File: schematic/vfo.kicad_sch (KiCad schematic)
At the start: 12 parts, among them U2 Si5351-module

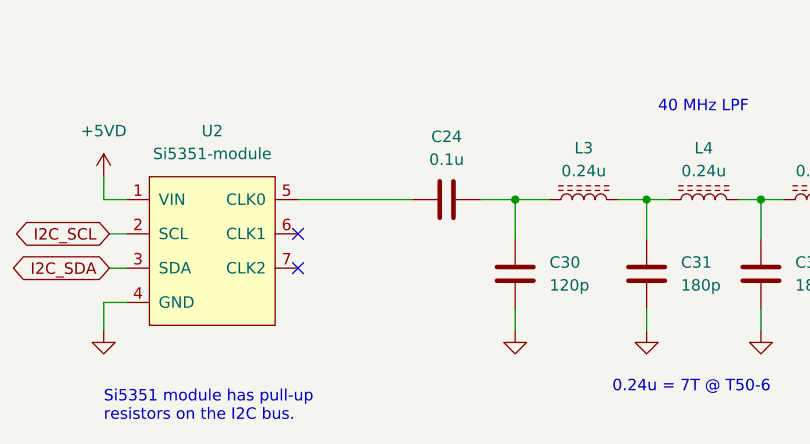
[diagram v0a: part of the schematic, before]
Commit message: Add CW tone generator + other changes
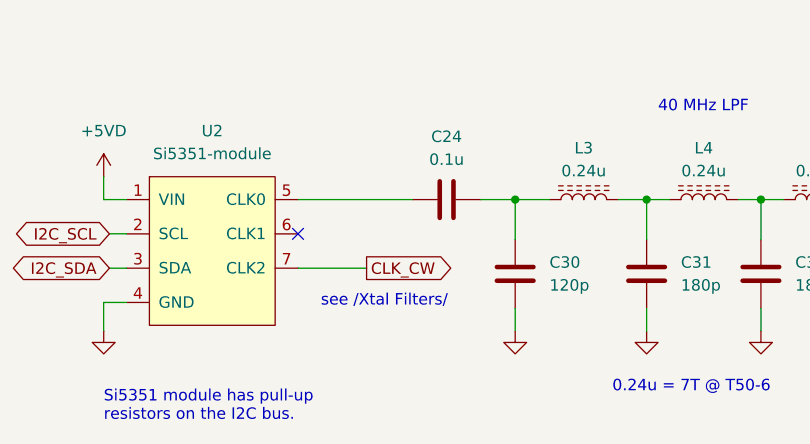
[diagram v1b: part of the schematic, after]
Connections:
- net CLK_CW: now reaches U2.7 (CLK2)
- no-connect marks 2 -> 1
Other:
- note added: "see /Xtal Filters/"
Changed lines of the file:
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@@
   )
   (no_connect (at 98.425 104.775))
-  (no_connect (at 98.425 108.585))
   (wire (pts (xy 98.425 100.965) (xy 111.125 100.965))
     (stroke (width 0) (type default))
@@
     (stroke (width 0) (type default))
   )
+  (wire (pts (xy 98.425 108.585) (xy 106.045 108.585))
+    (stroke (width 0) (type default))
+  )
   (wire (pts (xy 122.555 100.965) (xy 122.555 105.41))
     (stroke (width 0) (type default))
@@
     (effects (font (size 1.27 1.27)) (justify left bottom))
   )
+  (text "see /Xtal Filters/" (at 100.965 113.03 0)
+    (effects (font (size 1.27 1.27)) (justify left bottom))
+  )
   (text "0.24u = 7T @ T50-6" (at 133.35 122.555 0)
     (effects (font (size 1.27 1.27)) (justify left bottom))
@@
     (effects (font (size 1.27 1.27)) (justify left bottom))
   )
+  (global_label "CLK_CW" (shape output) (at 106.045 108.585 0) (fields_autoplaced)
+    (effects (font (size 1.27 1.27)) (justify left))
+    (property "Intersheetrefs" "${INTERSHEET_REFS}" (at 116.2079 108.585 0)
+      (effects (font (size 1.27 1.27)) (justify left) hide)
+    )
+  )
   (global_label "VFO_TX" (shape output) (at 208.28 103.505 0) (fields_autoplaced)

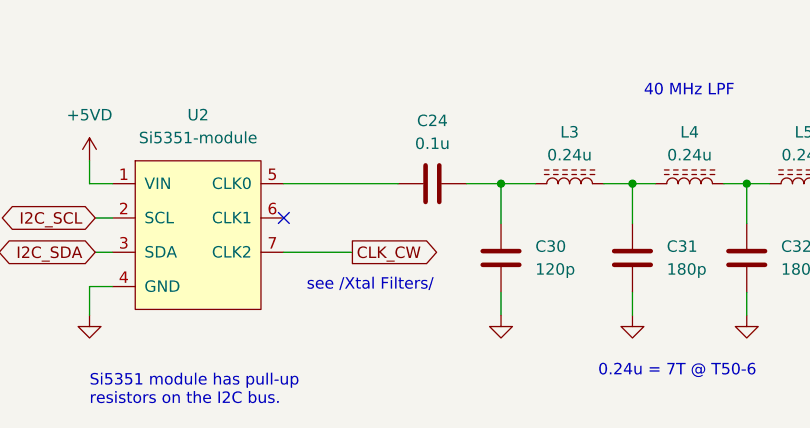
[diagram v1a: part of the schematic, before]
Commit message: Schematic: minor changes
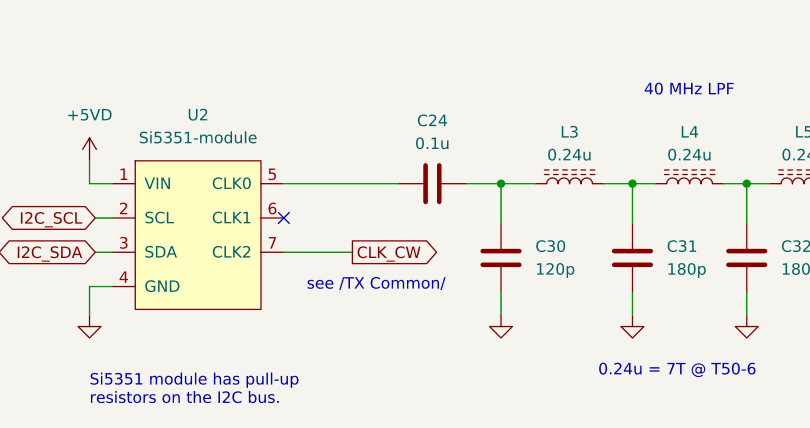
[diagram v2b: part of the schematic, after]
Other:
- note added: "see /TX Common/"
- note removed: "see /Xtal Filters/"
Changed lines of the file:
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@@
     (effects (font (size 1.27 1.27)) (justify left bottom))
   )
-  (text "see /Xtal Filters/" (at 100.965 113.03 0)
+  (text "see /TX Common/" (at 100.965 113.03 0)
     (effects (font (size 1.27 1.27)) (justify left bottom))
   )

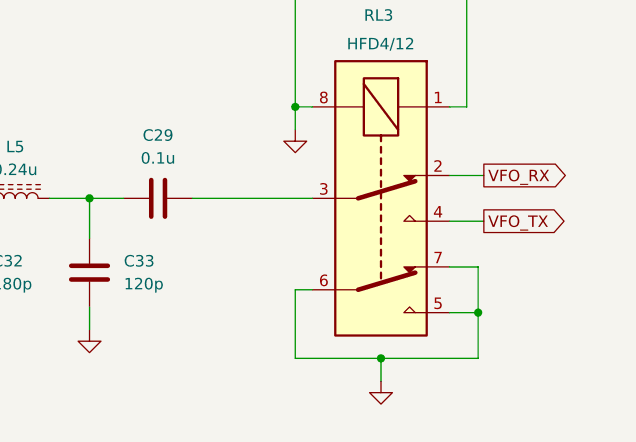
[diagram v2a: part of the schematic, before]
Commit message: Connect relay contact groups in parallel where appropriate
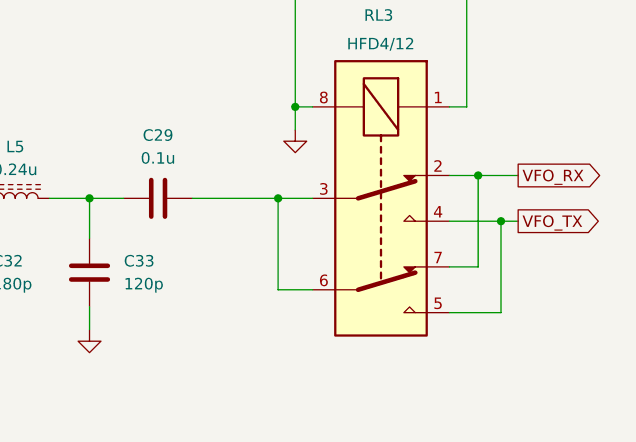
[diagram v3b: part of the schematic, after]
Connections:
- net GND: no longer RL3.5, RL3.6, RL3.7
- net VFO_RX: now also RL3.7
- net VFO_TX: now also RL3.5
- net at C29.2, RL3.3: now also RL3.6
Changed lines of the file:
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@@
   (junction (at 164.465 100.965) (diameter 0) (color 0 0 0 0)
   )
+  (junction (at 185.42 100.965) (diameter 0) (color 0 0 0 0)
+  )
+  (junction (at 207.645 98.425) (diameter 0) (color 0 0 0 0)
+  )
   (junction (at 122.555 100.965) (diameter 0) (color 0 0 0 0)
   )
-  (junction (at 196.85 118.745) (diameter 0) (color 0 0 0 0)
-  )
   (junction (at 137.16 100.965) (diameter 0) (color 0 0 0 0)
   )
+  (junction (at 210.185 103.505) (diameter 0) (color 0 0 0 0)
+  )
   (junction (at 206.375 76.2) (diameter 0) (color 0 0 0 0)
-  )
-  (junction (at 207.645 113.665) (diameter 0) (color 0 0 0 0)
   )
   (junction (at 187.325 90.805) (diameter 0) (color 0 0 0 0)
@@
     (stroke (width 0) (type default))
   )
-  (wire (pts (xy 204.47 113.665) (xy 207.645 113.665))
+  (wire (pts (xy 207.645 98.425) (xy 207.645 108.585))
+    (stroke (width 0) (type default))
+  )
+  (wire (pts (xy 204.47 113.665) (xy 210.185 113.665))
     (stroke (width 0) (type default))
   )
@@
     (stroke (width 0) (type default))
   )
-  (wire (pts (xy 207.645 113.665) (xy 207.645 108.585))
-    (stroke (width 0) (type default))
-  )
-  (wire (pts (xy 175.895 100.965) (xy 189.23 100.965))
+  (wire (pts (xy 175.895 100.965) (xy 185.42 100.965))
+    (stroke (width 0) (type default))
+  )
+  (wire (pts (xy 207.645 98.425) (xy 212.09 98.425))
     (stroke (width 0) (type default))
   )
@@
     (stroke (width 0) (type default))
   )
-  (wire (pts (xy 196.85 118.745) (xy 207.645 118.745))
-    (stroke (width 0) (type default))
-  )
   (wire (pts (xy 206.375 62.23) (xy 206.375 76.2))
     (stroke (width 0) (type default))
   )
-  (wire (pts (xy 187.325 118.745) (xy 187.325 111.125))
-    (stroke (width 0) (type default))
-  )
   (wire (pts (xy 206.375 62.23) (xy 210.82 62.23))
     (stroke (width 0) (type default))
@@
     (stroke (width 0) (type default))
   )
+  (wire (pts (xy 210.185 113.665) (xy 210.185 103.505))
+    (stroke (width 0) (type default))
+  )
   (wire (pts (xy 122.555 113.03) (xy 122.555 115.57))
     (stroke (width 0) (type default))
@@
     (stroke (width 0) (type default))
   )
-  (wire (pts (xy 196.85 121.285) (xy 196.85 118.745))
+  (wire (pts (xy 210.185 103.505) (xy 212.09 103.505))
+    (stroke (width 0) (type default))
+  )
+  (wire (pts (xy 185.42 100.965) (xy 189.23 100.965))
     (stroke (width 0) (type default))
   )
@@
     (stroke (width 0) (type default))
   )
-  (wire (pts (xy 187.325 111.125) (xy 189.23 111.125))
-    (stroke (width 0) (type default))
-  )
-  (wire (pts (xy 196.85 118.745) (xy 187.325 118.745))
-    (stroke (width 0) (type default))
-  )
-  (wire (pts (xy 204.47 98.425) (xy 208.28 98.425))
+  (wire (pts (xy 185.42 100.965) (xy 185.42 111.125))
+    (stroke (width 0) (type default))
+  )
+  (wire (pts (xy 185.42 111.125) (xy 189.23 111.125))
+    (stroke (width 0) (type default))
+  )
+  (wire (pts (xy 204.47 98.425) (xy 207.645 98.425))
     (stroke (width 0) (type default))
   )
@@
     (stroke (width 0) (type default))
   )
-  (wire (pts (xy 207.645 118.745) (xy 207.645 113.665))
-    (stroke (width 0) (type default))
-  )
-  (wire (pts (xy 204.47 103.505) (xy 208.28 103.505))
+  (wire (pts (xy 204.47 103.505) (xy 210.185 103.505))
     (stroke (width 0) (type default))
   )
@@
     )
   )
-  (global_label "VFO_TX" (shape output) (at 208.28 103.505 0) (fields_autoplaced)
-    (effects (font (size 1.27 1.27)) (justify left))
-    (property "Intersheetrefs" "${INTERSHEET_REFS}" (at 217.8382 103.505 0)
+  (global_label "VFO_TX" (shape output) (at 212.09 103.505 0) (fields_autoplaced)
+    (effects (font (size 1.27 1.27)) (justify left))
+    (property "Intersheetrefs" "${INTERSHEET_REFS}" (at 221.6482 103.505 0)
       (effects (font (size 1.27 1.27)) (justify left) hide)
     )
@@
     )
   )
-  (global_label "VFO_RX" (shape output) (at 208.28 98.425 0) (fields_autoplaced)
-    (effects (font (size 1.27 1.27)) (justify left))
-    (property "Intersheetrefs" "${INTERSHEET_REFS}" (at 218.1406 98.425 0)
-      (effects (font (size 1.27 1.27)) (justify left) hide)
-    )
-  )
-  (symbol (lib_id "power:GND") (at 196.85 121.285 0) (unit 1)
-    (in_bom yes) (on_board yes) (dnp no) (fields_autoplaced)
-    (property "Reference" "#PWR0127" (at 196.85 127.635 0)
-      (effects (font (size 1.27 1.27)) hide)
-    )
-    (property "Value" "GND" (at 196.85 126.365 0)
-      (effects (font (size 1.27 1.27)) hide)
-    )
-    (property "Footprint" "" (at 196.85 121.285 0)
-      (effects (font (size 1.27 1.27)) hide)
-    )
-    (property "Datasheet" "" (at 196.85 121.285 0)
-      (effects (font (size 1.27 1.27)) hide)
-    )
-    (pin "1")
-    (instances
-      (project "hbr-mk2"
-        (path "/700c9878-4ed7-49d5-a273-77cf9d92989d/4a33e42c-b3be-4c3a-afde-bb63d1cdac9b"
-          (reference "#PWR0127") (unit 1)
-        )
-        (path "/700c9878-4ed7-49d5-a273-77cf9d92989d/f4ed3a4d-9175-4bdf-997e-86328a748647"
-          (reference "#PWR0127") (unit 1)
-        )
-      )
-    )
-  )
+  (global_label "VFO_RX" (shape output) (at 212.09 98.425 0) (fields_autoplaced)
+    (effects (font (size 1.27 1.27)) (justify left))
+    (property "Intersheetrefs" "${INTERSHEET_REFS}" (at 221.9506 98.425 0)
+      (effects (font (size 1.27 1.27)) (justify left) hide)
+    )
+  )

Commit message: Schematic: minor fixes
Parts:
- L3, L4, L5: value 0.24u -> T50-6
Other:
- note added: "0.24u"
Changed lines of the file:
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@@
+    (effects (font (size 1.27 1.27)) (justify left bottom))
+  )
+  (text "0.24u" (at 140.97 98.425 0)
     (effects (font (size 1.27 1.27)) (justify left bottom))
   )
@@
     (effects (font (size 1.27 1.27)) (justify left bottom))
   )
+  (text "0.24u" (at 127.635 98.425 0)
+    (effects (font (size 1.27 1.27)) (justify left bottom))
+  )
   (text "0.24u = 7T @ T50-6" (at 133.35 122.555 0)
+    (effects (font (size 1.27 1.27)) (justify left bottom))
+  )
+  (text "0.24u" (at 153.67 98.425 0)
     (effects (font (size 1.27 1.27)) (justify left bottom))
   )
@@
       (effects (font (size 1.27 1.27)))
     )
-    (property "Value" "0.24u" (at 156.21 97.79 90)
-      (effects (font (size 1.27 1.27)))
+    (property "Value" "T50-6" (at 156.21 97.79 90)
+      (effects (font (size 1.27 1.27)) hide)
     )
     (property "Footprint" "" (at 156.21 100.965 0)
@@
       (effects (font (size 1.27 1.27)))
     )
-    (property "Value" "0.24u" (at 130.175 97.79 90)
-      (effects (font (size 1.27 1.27)))
+    (property "Value" "T50-6" (at 130.175 97.79 90)
+      (effects (font (size 1.27 1.27)) hide)
     )
     (property "Footprint" "" (at 130.175 100.965 0)
@@
       (effects (font (size 1.27 1.27)))
     )
-    (property "Value" "0.24u" (at 143.51 97.79 90)
-      (effects (font (size 1.27 1.27)))
+    (property "Value" "T50-6" (at 143.51 97.79 90)
+      (effects (font (size 1.27 1.27)) hide)
     )
     (property "Footprint" "" (at 143.51 100.965 0)

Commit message: Minor changes
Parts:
- renumbered C24 to C59, C30 to C60, C31 to C61, C32 to C62, C33 to C63, C29 to C64, L3 to L6, L4 to L7, L5 to L8, RL3 to RL7
